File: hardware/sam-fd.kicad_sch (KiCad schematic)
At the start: 6 parts

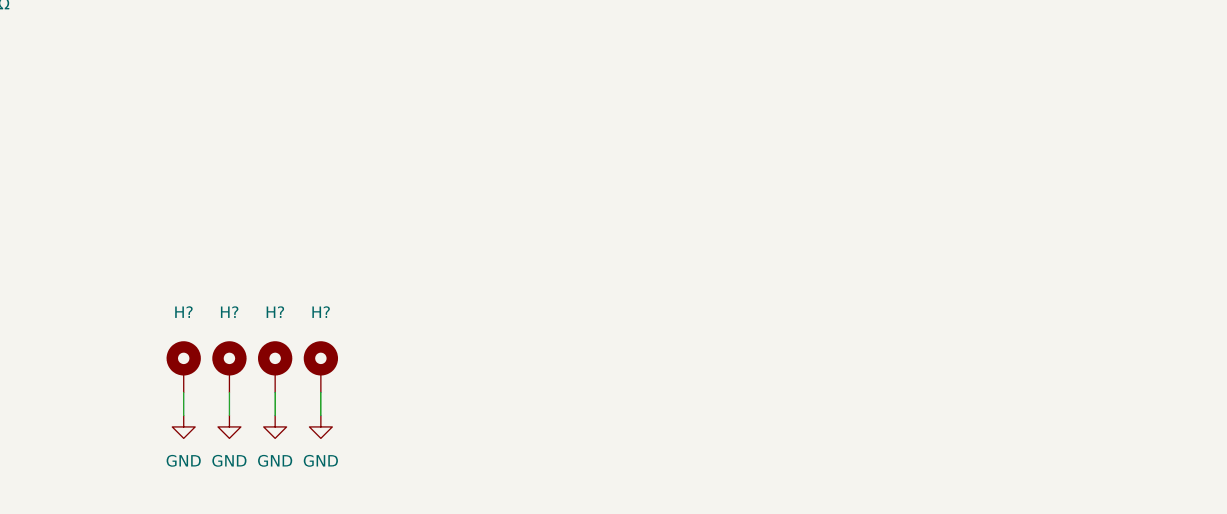
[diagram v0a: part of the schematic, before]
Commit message: add can transceiver
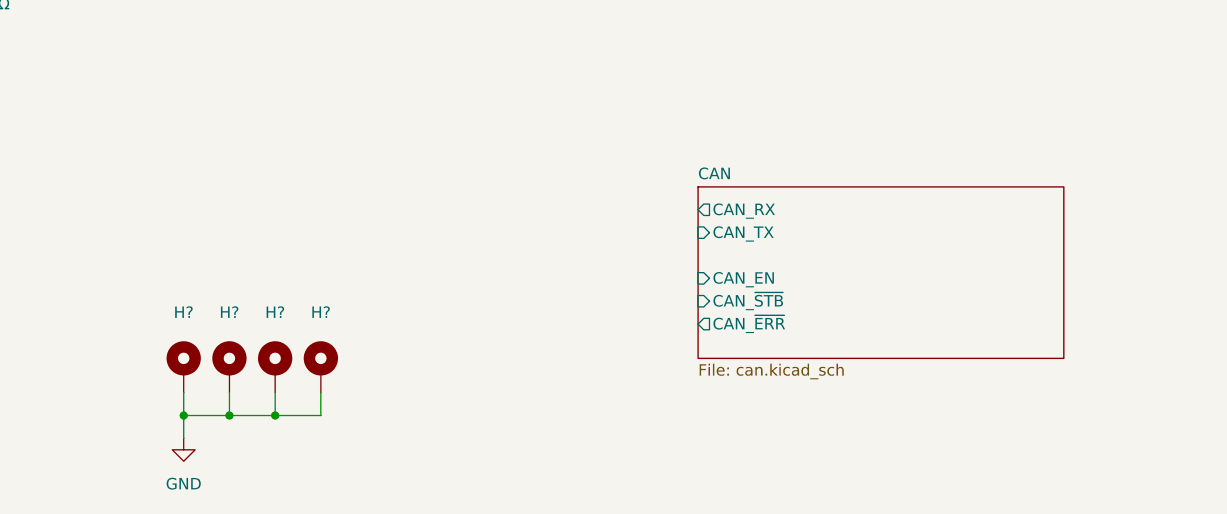
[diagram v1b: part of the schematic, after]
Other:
- added sheet CAN (can.kicad_sch)

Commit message: worked on it
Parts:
- added D2, D3: GREEN, LED_SMD:LED_0603_1608Metric, symbol Device:LED
- added R2, R3: 68Ω, Resistor_SMD:R_0402_1005Metric, symbol Device:R
- D1: renamed from D?; footprint (none) -> LED_SMD:LED_0603_1608Metric; Mfr. (none) -> Lite-On; Mfr. No (none) -> LTST-C190KRKT; Mouser No (none) -> 859-LTST-C190KRKT
- H1, H2, H3, H4: renamed from H?; footprint (none) -> MountingHole:MountingHole_2.7mm_M2.5_Pad_Via
- R1: renamed from R?; footprint (none) -> Resistor_SMD:R_0402_1005Metric; Mfr. (none) -> YAGEO; Mfr. No (none) -> RC0402FR-0768RL; Mouser No (none) -> 603-RC0402FR-0768RL
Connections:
- net +3V3: now also D2.2 (A), D3.2 (A)
- new net: D3.1 (K), R3.1
- new net: D2.1 (K), R2.1
- new net RX_ACT: R2.2
- new net TX_ACT: R3.2
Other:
- moved on the sheet: D1, H1, H2, H3, H4, R1

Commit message: did a little routing
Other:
- note added: "TODO: ROUTE UART RX/TX"
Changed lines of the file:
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@@
     (stroke (width 0) (type default) (color 0 0 0 0))
+  )
+  (text "TODO: ROUTE UART RX/TX" (at 152.4 113.03 0)
+    (effects (font (size 1.27 1.27)) (justify left bottom))
   )
   (label "CAN_RX" (at 140.97 73.66 0)

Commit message: ordered, pray this works
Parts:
- H1, H2, H3, H4: footprint MountingHole:MountingHole_2.7mm_M2.5_Pad_Via -> MountingHole:MountingHole_2.2mm_M2_Pad_Via
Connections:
- net RX_ACT: now also R3.2; no longer R2.2
- net TX_ACT: now also R2.2; no longer R3.2
- no-connect marks 0 -> 11
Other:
- note removed: "TODO: ROUTE UART RX/TX"
- company: (none) -> Leon Rinkel
- title: (none) -> sam-fd
- moved on the sheet: D1, D2, D3, H1, H2, H3, H4, R1, R2, R3

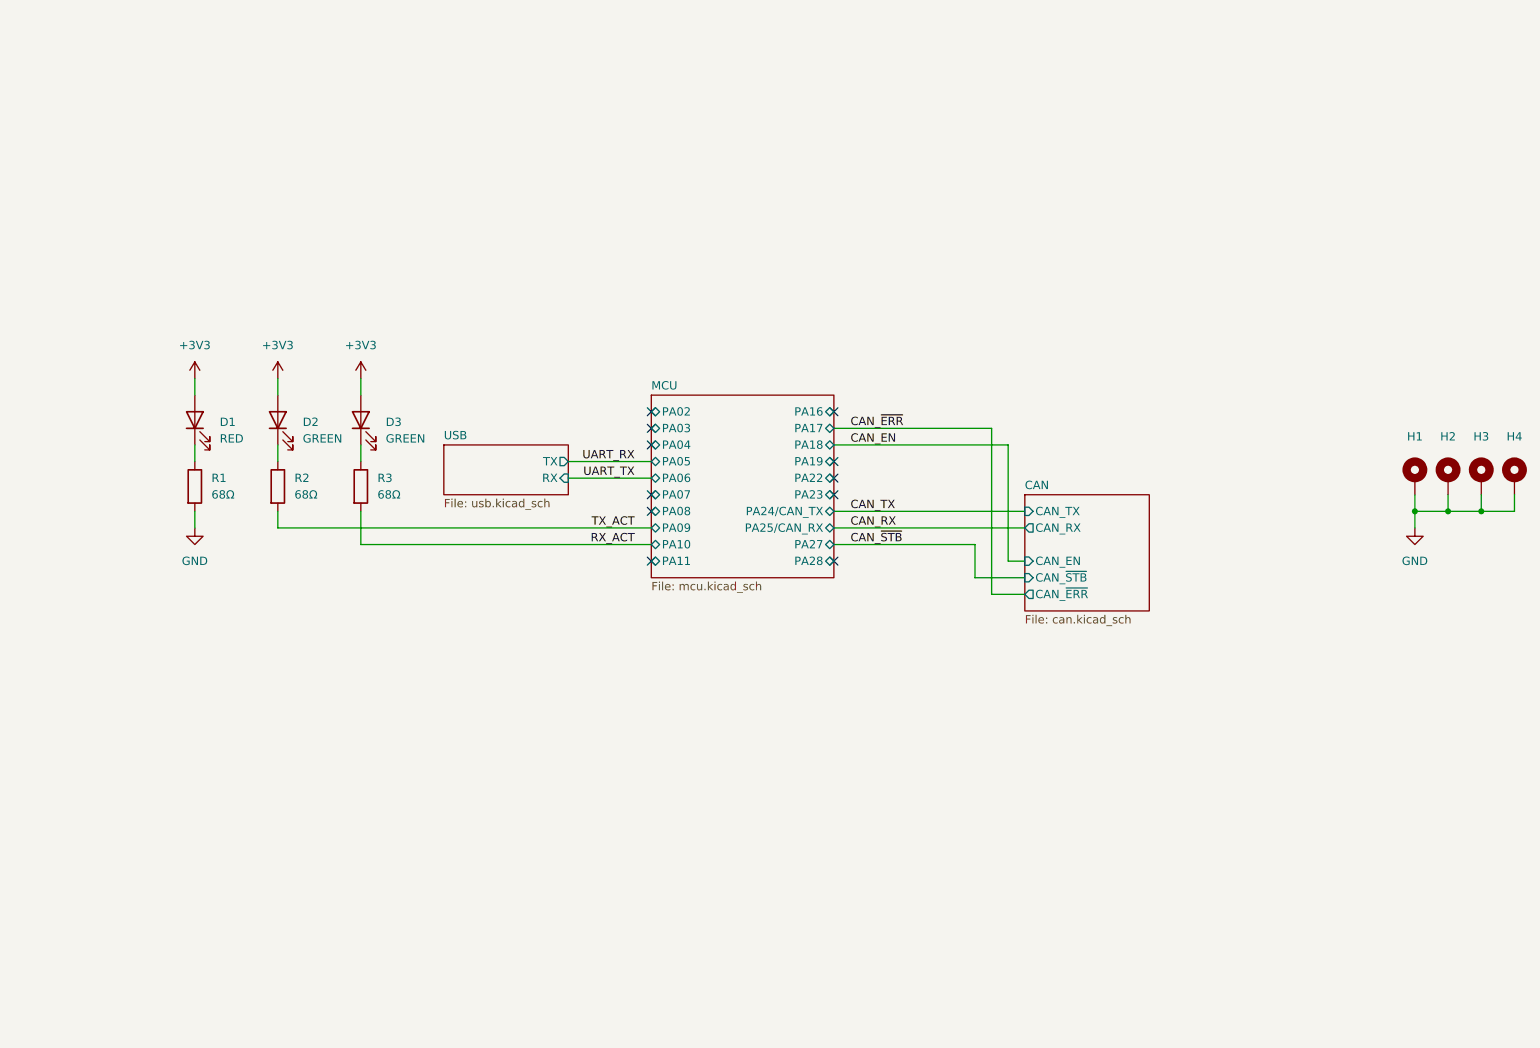
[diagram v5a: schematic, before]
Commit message: leds through transistor, castellated holes
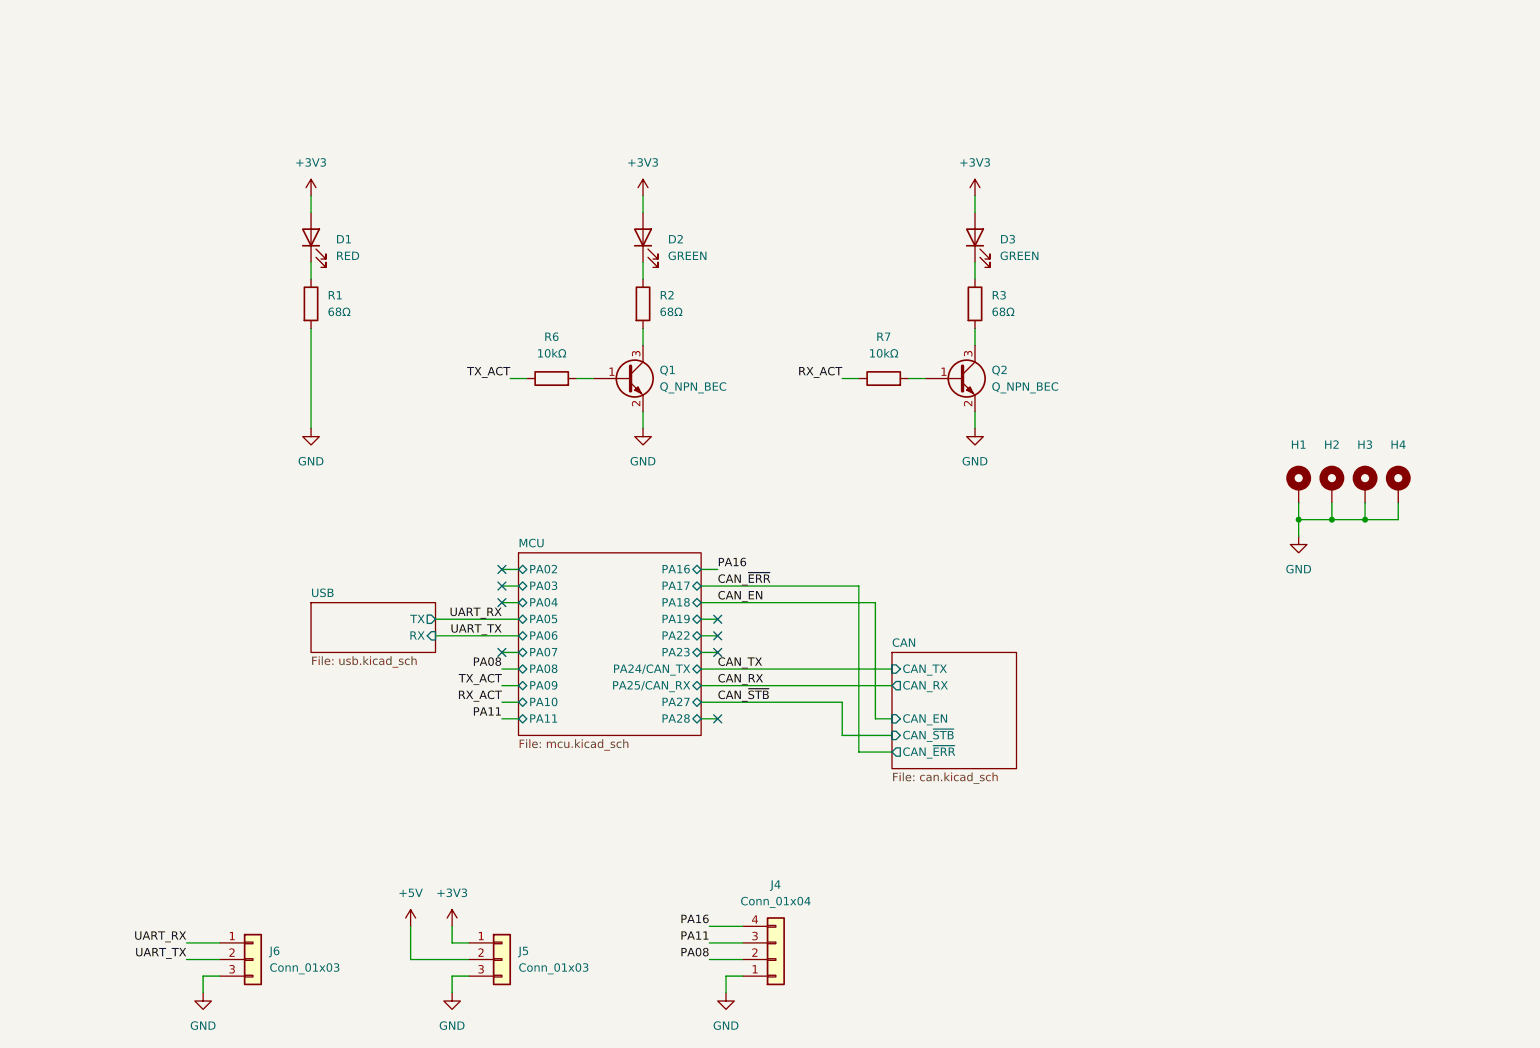
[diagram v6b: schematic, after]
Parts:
- added J4: Conn_01x04, sam-fd:CastellatedHoles_1x04_P2.54mm, symbol Connector_Generic:Conn_01x04
- added J5, J6: Conn_01x03, sam-fd:CastellatedHoles_1x03_P2.54mm, symbol Connector_Generic:Conn_01x03
- added Q1, Q2: Q_NPN_BEC, Package_TO_SOT_SMD:SOT-23, symbol Device:Q_NPN_BEC
- added R6, R7: 10kΩ, Resistor_SMD:R_0402_1005Metric, symbol Device:R
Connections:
- net +3V3: now also J5.1 (Pin_1)
- net GND: now also J4.1 (Pin_1), J5.3 (Pin_3), J6.3 (Pin_3), Q1.2 (E), Q2.2 (E)
- net RX_ACT: now also R7.1; no longer R3.2
- net TX_ACT: now also R6.1; no longer R2.2
- net UART_RX: now also J6.1 (Pin_1)
- net UART_TX: now also J6.2 (Pin_2)
- new net: Q2.3 (C), R3.2
- new net: Q2.1 (B), R7.2
- new net: Q1.1 (B), R6.2
- new net: Q1.3 (C), R2.2
- new net +5V: J5.2 (Pin_2)
- new net PA08: J4.2 (Pin_2)
- new net PA11: J4.3 (Pin_3)
- new net PA16: J4.4 (Pin_4)
- no-connect marks 11 -> 8
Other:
- moved on the sheet: D1, D2, D3, H1, H2, H3, H4, R1, R2, R3
